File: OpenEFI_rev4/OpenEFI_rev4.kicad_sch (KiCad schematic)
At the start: 97 parts, among them J1 USB_B, J2 Tag connect, J3 104031-0811, J4 Conn_02x08_Odd_Even, Q1 AO3400A, Q11 SS8050, Q12 AO3400A, Q19 AO3400A, Q2 AO3400A, Q3 AO3400A, Q4 AO3400A, Q8 SS8050, Q9 SS8050, SW1 SW_Push, U11 SRV05-4, U15 REF3033, U23 PaP_Driver_v1, U25 TJA1051T-3, U3 STM32F407VGTx, U7 25LCxxx, Y1 25MHz, Y3 32.768kHz

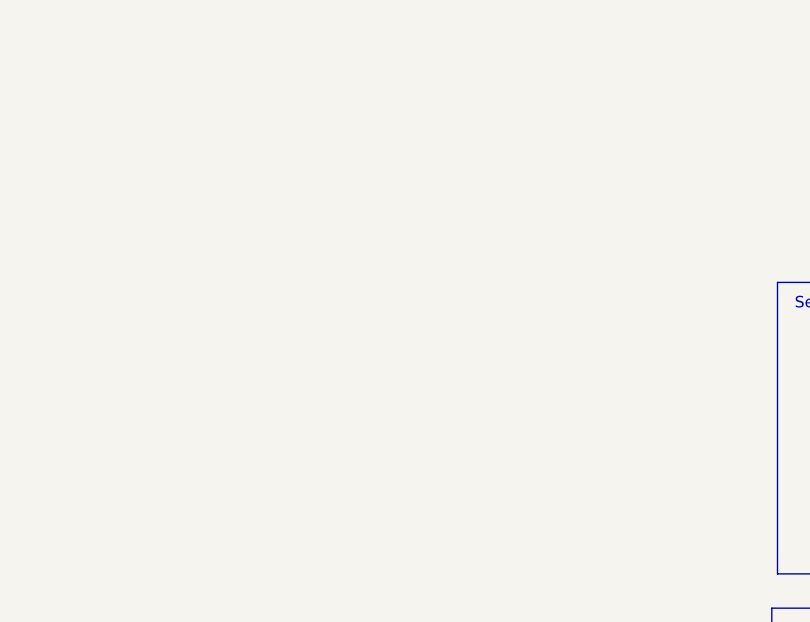
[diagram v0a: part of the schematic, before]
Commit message: fix pcb size/wideband
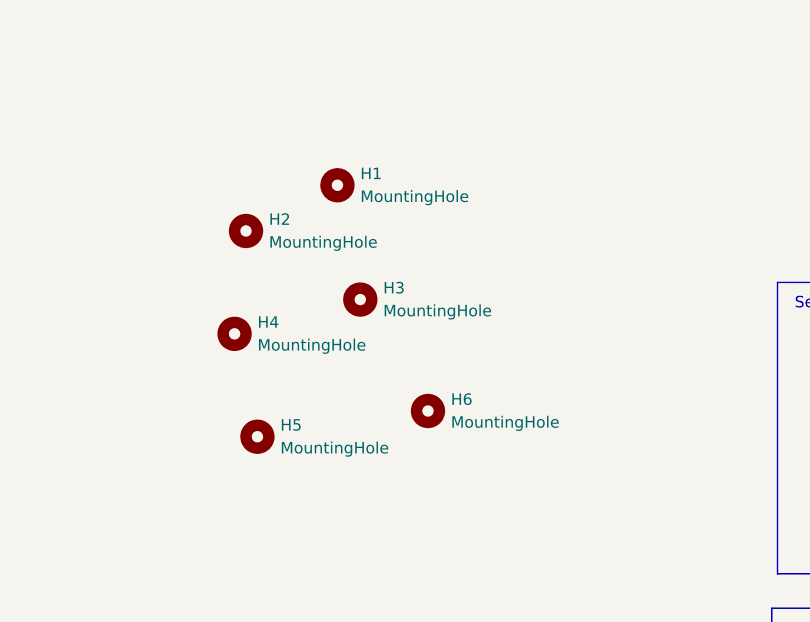
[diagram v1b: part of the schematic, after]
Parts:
- added H1, H2, H3, H4: MountingHole, MountingHole:MountingHole_3.5mm_Pad_Via, symbol Mechanical:MountingHole
- added H5, H6: MountingHole, MountingHole:MountingHole_2.1mm, symbol Mechanical:MountingHole
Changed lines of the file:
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@@
     )
   )
+  (symbol (lib_id "Mechanical:MountingHole") (at 257.81 102.87 0) (unit 1)
+    (in_bom yes) (on_board yes) (dnp no) (fields_autoplaced)
+    (property "Reference" "H3" (at 260.35 101.6 0)
+      (effects (font (size 1.27 1.27)) (justify left))
+    )
+    (property "Value" "MountingHole" (at 260.35 104.14 0)
+      (effects (font (size 1.27 1.27)) (justify left))
+    )
+    (property "Footprint" "MountingHole:MountingHole_3.5mm_Pad_Via" (at 257.81 102.87 0)
+      (effects (font (size 1.27 1.27)) hide)
+    )
+    (property "Datasheet" "~" (at 257.81 102.87 0)
+      (effects (font (size 1.27 1.27)) hide)
+    )
+    (instances
+      (project "OpenEFI_rev4"
+        (path "/b282ce4b-c3d0-4c94-b06c-73b92bb672a9"
+          (reference "H3") (unit 1)
+        )
+      )
+    )
+  )
   (symbol (lib_id "power:+3V3") (at 372.11 149.86 0) (unit 1)
     (in_bom yes) (on_board yes) (dnp no)
@@
     )
   )
+  (symbol (lib_id "Mechanical:MountingHole") (at 265.3277 115.2512 0) (unit 1)
+    (in_bom yes) (on_board yes) (dnp no) (fields_autoplaced)
+    (property "Reference" "H6" (at 267.8677 113.9812 0)
+      (effects (font (size 1.27 1.27)) (justify left))
+    )
+    (property "Value" "MountingHole" (at 267.8677 116.5212 0)
+      (effects (font (size 1.27 1.27)) (justify left))
+    )
+    (property "Footprint" "MountingHole:MountingHole_2.1mm" (at 265.3277 115.2512 0)
+      (effects (font (size 1.27 1.27)) hide)
+    )
+    (property "Datasheet" "~" (at 265.3277 115.2512 0)
+      (effects (font (size 1.27 1.27)) hide)
+    )
+    (instances
+      (project "OpenEFI_rev4"
+        (path "/b282ce4b-c3d0-4c94-b06c-73b92bb672a9"
+          (reference "H6") (unit 1)
+        )
+      )
+    )
+  )
   (symbol (lib_id "Device:R") (at 167.64 51.435 0) (mirror x) (unit 1)
     (in_bom yes) (on_board yes) (dnp no)
@@
     )
   )
+  (symbol (lib_id "Mechanical:MountingHole") (at 246.38 118.11 0) (unit 1)
+    (in_bom yes) (on_board yes) (dnp no) (fields_autoplaced)
+    (property "Reference" "H5" (at 248.92 116.84 0)
+      (effects (font (size 1.27 1.27)) (justify left))
+    )
+    (property "Value" "MountingHole" (at 248.92 119.38 0)
+      (effects (font (size 1.27 1.27)) (justify left))
+    )
+    (property "Footprint" "MountingHole:MountingHole_2.1mm" (at 246.38 118.11 0)
+      (effects (font (size 1.27 1.27)) hide)
+    )
+    (property "Datasheet" "~" (at 246.38 118.11 0)
+      (effects (font (size 1.27 1.27)) hide)
+    )
+    (instances
+      (project "OpenEFI_rev4"
+        (path "/b282ce4b-c3d0-4c94-b06c-73b92bb672a9"
+          (reference "H5") (unit 1)
+        )
+      )
+    )
+  )
   (symbol (lib_id "Connector:TestPoint") (at 321.31 206.375 0) (unit 1)
     (in_bom yes) (on_board yes) (dnp no)
@@
     )
   )
+  (symbol (lib_id "Mechanical:MountingHole") (at 245.11 95.25 0) (unit 1)
+    (in_bom yes) (on_board yes) (dnp no) (fields_autoplaced)
+    (property "Reference" "H2" (at 247.65 93.98 0)
+      (effects (font (size 1.27 1.27)) (justify left))
+    )
+    (property "Value" "MountingHole" (at 247.65 96.52 0)
+      (effects (font (size 1.27 1.27)) (justify left))
+    )
+    (property "Footprint" "MountingHole:MountingHole_3.5mm_Pad_Via" (at 245.11 95.25 0)
+      (effects (font (size 1.27 1.27)) hide)
+    )
+    (property "Datasheet" "~" (at 245.11 95.25 0)
+      (effects (font (size 1.27 1.27)) hide)
+    )
+    (instances
+      (project "OpenEFI_rev4"
+        (path "/b282ce4b-c3d0-4c94-b06c-73b92bb672a9"
+          (reference "H2") (unit 1)
+        )
+      )
+    )
+  )
   (symbol (lib_id "Jumper:SolderJumper_2_Open") (at 69.85 38.1 0) (unit 1)
     (in_bom yes) (on_board yes) (dnp no)
@@
     )
   )
+  (symbol (lib_id "Mechanical:MountingHole") (at 255.27 90.17 0) (unit 1)
+    (in_bom yes) (on_board yes) (dnp no) (fields_autoplaced)
+    (property "Reference" "H1" (at 257.81 88.9 0)
+      (effects (font (size 1.27 1.27)) (justify left))
+    )
+    (property "Value" "MountingHole" (at 257.81 91.44 0)
+      (effects (font (size 1.27 1.27)) (justify left))
+    )
+    (property "Footprint" "MountingHole:MountingHole_3.5mm_Pad_Via" (at 255.27 90.17 0)
+      (effects (font (size 1.27 1.27)) hide)
+    )
+    (property "Datasheet" "~" (at 255.27 90.17 0)
+      (effects (font (size 1.27 1.27)) hide)
+    )
+    (instances
+      (project "OpenEFI_rev4"
+        (path "/b282ce4b-c3d0-4c94-b06c-73b92bb672a9"
+          (reference "H1") (unit 1)
+        )
+      )
+    )
+  )
   (symbol (lib_id "Device:R_Pack04") (at 316.23 34.29 0) (unit 1)
     (in_bom yes) (on_board yes) (dnp no)
@@
         )
       )
+    )
+  )
+  (symbol (lib_id "Mechanical:MountingHole") (at 243.84 106.68 0) (unit 1)
+    (in_bom yes) (on_board yes) (dnp no) (fields_autoplaced)
+    (property "Reference" "H4" (at 246.38 105.41 0)
+      (effects (font (size 1.27 1.27)) (justify left))
+    )
+    (property "Value" "MountingHole" (at 246.38 107.95 0)
+      (effects (font (size 1.27 1.27)) (justify left))
+    )
+    (property "Footprint" "MountingHole:MountingHole_3.5mm_Pad_Via" (at 243.84 106.68 0)
+      (effects (font (size 1.27 1.27)) hide)
+    )
+    (property "Datasheet" "~" (at 243.84 106.68 0)
+      (effects (font (size 1.27 1.27)) hide)
+    )
+    (instances
+      (project "OpenEFI_rev4"
+        (path "/b282ce4b-c3d0-4c94-b06c-73b92bb672a9"
+          (reference "H4") (unit 1)
+        )
+      )

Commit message: WIP Rev4 SPI
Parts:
- BT1: now left out of the parts list
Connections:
- net AUX_IN_6: now also U3.93 (PB7); no longer U3.98 (PE1)
- net AUX_IN_7: now also U3.95 (PB8); no longer U3.93 (PB7)
- net AUX_IN_8: now also U3.98 (PE1); no longer U3.95 (PB8)
- net SD_CD: now also RN5.4 (R4.1); no longer RN6.2 (R2.1)
- net SD_CMD: now also RN5.1 (R1.1); no longer RN5.2 (R2.1)
- net SD_DAT1: now also RN6.2 (R2.1); no longer RN5.1 (R1.1)
- net SD_DAT2: now also RN5.3 (R3.1); no longer RN5.4 (R4.1)
- net SD_DAT3: now also RN5.2 (R2.1); no longer RN5.3 (R3.1)
- net SPI2_MISO: now also J4.8 (Pin_8); no longer J4.6 (Pin_6)
- net SPI2_MOSI: now also J4.6 (Pin_6); no longer J4.8 (Pin_8)
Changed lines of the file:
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@@
     (effects (font (size 0.889 0.889)) (justify right bottom))
   )
-  (label "SD_DAT2" (at 334.01 38.1 270) (fields_autoplaced)
+  (label "SD_DAT2" (at 331.47 38.1 270) (fields_autoplaced)
     (effects (font (size 0.7874 0.7874)) (justify right bottom))
   )
@@
     (effects (font (size 0.8 0.8)) (justify left bottom))
   )
-  (label "SPI2_MISO" (at 323.85 226.06 0) (fields_autoplaced)
+  (label "SPI2_MISO" (at 323.85 228.6 0) (fields_autoplaced)
     (effects (font (size 0.7874 0.7874)) (justify left bottom))
   )
@@
     (effects (font (size 0.7874 0.7874)) (justify left bottom))
   )
-  (label "AUX_IN_6" (at 142.24 151.13 180) (fields_autoplaced)
-    (effects (font (size 0.889 0.889)) (justify right bottom))
+  (label "AUX_IN_6" (at 193.04 166.37 0) (fields_autoplaced)
+    (effects (font (size 0.889 0.889)) (justify left bottom))
   )
   (label "MUX_A" (at 142.24 199.39 180) (fields_autoplaced)
@@
     (effects (font (size 0.7874 0.7874)) (justify left bottom))
   )
-  (label "AUX_IN_8" (at 193.04 168.91 0) (fields_autoplaced)
-    (effects (font (size 0.889 0.889)) (justify left bottom))
+  (label "AUX_IN_8" (at 142.24 151.13 180) (fields_autoplaced)
+    (effects (font (size 0.889 0.889)) (justify right bottom))
   )
   (label "ECN2" (at 401.32 118.11 180) (fields_autoplaced)
@@
     (effects (font (size 1.27 1.27)) (justify right bottom))
   )
-  (label "SPI2_MOSI" (at 323.85 228.6 0) (fields_autoplaced)
+  (label "SPI2_MOSI" (at 323.85 226.06 0) (fields_autoplaced)
     (effects (font (size 0.7874 0.7874)) (justify left bottom))
   )
@@
     (effects (font (size 0.7874 0.7874)) (justify left bottom))
   )
-  (label "SD_CMD" (at 328.93 38.1 270) (fields_autoplaced)
+  (label "SD_CMD" (at 326.39 38.1 270) (fields_autoplaced)
     (effects (font (size 0.7874 0.7874)) (justify right bottom))
   )
@@
     (effects (font (size 0.9906 0.9906)) (justify left bottom))
   )
-  (label "AUX_IN_7" (at 193.04 166.37 0) (fields_autoplaced)
+  (label "AUX_IN_7" (at 193.04 168.91 0) (fields_autoplaced)
     (effects (font (size 0.889 0.889)) (justify left bottom))
   )
@@
     (effects (font (size 0.889 0.889)) (justify left bottom))
   )
-  (label "SD_DAT1" (at 326.39 38.1 270) (fields_autoplaced)
+  (label "SD_DAT1" (at 313.69 39.37 270) (fields_autoplaced)
     (effects (font (size 0.7874 0.7874)) (justify right bottom))
   )
@@
     (effects (font (size 0.889 0.889)) (justify right bottom))
   )
-  (label "SD_DAT3" (at 331.47 38.1 270) (fields_autoplaced)
+  (label "SD_DAT3" (at 328.93 38.1 270) (fields_autoplaced)
     (effects (font (size 0.7874 0.7874)) (justify right bottom))
   )
@@
     (effects (font (size 0.9906 0.9906)) (justify left bottom))
   )
-  (label "SD_CD" (at 313.69 39.37 270) (fields_autoplaced)
+  (label "SD_CD" (at 334.01 38.1 270) (fields_autoplaced)
     (effects (font (size 0.889 0.889)) (justify right bottom))
   )
@@
     )
   )
-  (symbol (lib_id "Mechanical:MountingHole") (at 257.81 102.87 0) (unit 1)
+  (symbol (lib_id "Mechanical:MountingHole") (at 290.83 177.165 0) (unit 1)
     (in_bom yes) (on_board yes) (dnp no) (fields_autoplaced)
-    (property "Reference" "H3" (at 260.35 101.6 0)
-      (effects (font (size 1.27 1.27)) (justify left))
+    (property "Reference" "H3" (at 293.37 175.895 0)
+      (effects (font (size 1.27 1.27)) (justify left) hide)
     )
-    (property "Value" "MountingHole" (at 260.35 104.14 0)
-      (effects (font (size 1.27 1.27)) (justify left))
+    (property "Value" "MountingHole" (at 293.37 178.435 0)
+      (effects (font (size 1.27 1.27)) (justify left) hide)
     )
-    (property "Footprint" "MountingHole:MountingHole_3.5mm_Pad_Via" (at 257.81 102.87 0)
+    (property "Footprint" "MountingHole:MountingHole_3.5mm_Pad_Via" (at 290.83 177.165 0)
       (effects (font (size 1.27 1.27)) hide)
     )
-    (property "Datasheet" "~" (at 257.81 102.87 0)
+    (property "Datasheet" "~" (at 290.83 177.165 0)
       (effects (font (size 1.27 1.27)) hide)
     )
@@
     )
   )
-  (symbol (lib_id "Mechanical:MountingHole") (at 265.3277 115.2512 0) (unit 1)
+  (symbol (lib_id "Mechanical:MountingHole") (at 290.83 172.72 0) (unit 1)
     (in_bom yes) (on_board yes) (dnp no) (fields_autoplaced)
-    (property "Reference" "H6" (at 267.8677 113.9812 0)
-      (effects (font (size 1.27 1.27)) (justify left))
+    (property "Reference" "H6" (at 293.37 172.72 0)
+      (effects (font (size 1.27 1.27)) (justify left) hide)
     )
-    (property "Value" "MountingHole" (at 267.8677 116.5212 0)
-      (effects (font (size 1.27 1.27)) (justify left))
+    (property "Value" "MountingHole" (at 293.37 173.99 0)
+      (effects (font (size 1.27 1.27)) (justify left) hide)
     )
-    (property "Footprint" "MountingHole:MountingHole_2.1mm" (at 265.3277 115.2512 0)
+    (property "Footprint" "MountingHole:MountingHole_2.1mm" (at 290.83 172.72 0)
       (effects (font (size 1.27 1.27)) hide)
     )
-    (property "Datasheet" "~" (at 265.3277 115.2512 0)
+    (property "Datasheet" "~" (at 290.83 172.72 0)
       (effects (font (size 1.27 1.27)) hide)
     )
@@
     )
   )
-  (symbol (lib_id "Mechanical:MountingHole") (at 246.38 118.11 0) (unit 1)
+  (symbol (lib_id "Mechanical:MountingHole") (at 286.385 177.165 0) (unit 1)
     (in_bom yes) (on_board yes) (dnp no) (fields_autoplaced)
-    (property "Reference" "H5" (at 248.92 116.84 0)
-      (effects (font (size 1.27 1.27)) (justify left))
+    (property "Reference" "H5" (at 290.0927 177.165 0)
+      (effects (font (size 1.27 1.27)) (justify left) hide)
     )
-    (property "Value" "MountingHole" (at 248.92 119.38 0)
-      (effects (font (size 1.27 1.27)) (justify left))
+    (property "Value" "MountingHole" (at 288.925 178.435 0)
+      (effects (font (size 1.27 1.27)) (justify left) hide)
     )
-    (property "Footprint" "MountingHole:MountingHole_2.1mm" (at 246.38 118.11 0)
+    (property "Footprint" "MountingHole:MountingHole_2.1mm" (at 286.385 177.165 0)
       (effects (font (size 1.27 1.27)) hide)
     )
-    (property "Datasheet" "~" (at 246.38 118.11 0)
+    (property "Datasheet" "~" (at 286.385 177.165 0)
       (effects (font (size 1.27 1.27)) hide)
     )
@@
     )
   )
-  (symbol (lib_id "Mechanical:MountingHole") (at 245.11 95.25 0) (unit 1)
+  (symbol (lib_id "Mechanical:MountingHole") (at 286.385 168.275 0) (unit 1)
     (in_bom yes) (on_board yes) (dnp no) (fields_autoplaced)
-    (property "Reference" "H2" (at 247.65 93.98 0)
-      (effects (font (size 1.27 1.27)) (justify left))
+    (property "Reference" "H2" (at 288.925 167.005 0)
+      (effects (font (size 1.27 1.27)) (justify left) hide)
     )
-    (property "Value" "MountingHole" (at 247.65 96.52 0)
-      (effects (font (size 1.27 1.27)) (justify left))
+    (property "Value" "MountingHole" (at 288.925 169.545 0)
+      (effects (font (size 1.27 1.27)) (justify left) hide)
     )
-    (property "Footprint" "MountingHole:MountingHole_3.5mm_Pad_Via" (at 245.11 95.25 0)
+    (property "Footprint" "MountingHole:MountingHole_3.5mm_Pad_Via" (at 286.385 168.275 0)
       (effects (font (size 1.27 1.27)) hide)
     )
-    (property "Datasheet" "~" (at 245.11 95.25 0)
+    (property "Datasheet" "~" (at 286.385 168.275 0)
       (effects (font (size 1.27 1.27)) hide)
     )
@@
     )
   )
-  (symbol (lib_id "Mechanical:MountingHole") (at 255.27 90.17 0) (unit 1)
+  (symbol (lib_id "Mechanical:MountingHole") (at 290.83 168.275 0) (unit 1)
     (in_bom yes) (on_board yes) (dnp no) (fields_autoplaced)
-    (property "Reference" "H1" (at 257.81 88.9 0)
-      (effects (font (size 1.27 1.27)) (justify left))
+    (property "Reference" "H1" (at 293.37 167.005 0)
+      (effects (font (size 1.27 1.27)) (justify left) hide)
     )
-    (property "Value" "MountingHole" (at 257.81 91.44 0)
-      (effects (font (size 1.27 1.27)) (justify left))
+    (property "Value" "MountingHole" (at 293.37 169.545 0)
+      (effects (font (size 1.27 1.27)) (justify left) hide)
     )
-    (property "Footprint" "MountingHole:MountingHole_3.5mm_Pad_Via" (at 255.27 90.17 0)
+    (property "Footprint" "MountingHole:MountingHole_3.5mm_Pad_Via" (at 290.83 168.275 0)
       (effects (font (size 1.27 1.27)) hide)
     )
-    (property "Datasheet" "~" (at 255.27 90.17 0)
+    (property "Datasheet" "~" (at 290.83 168.275 0)
       (effects (font (size 1.27 1.27)) hide)
     )
@@
   )
   (symbol (lib_id "Device:Battery_Cell") (at 151.13 92.71 0) (unit 1)
-    (in_bom yes) (on_board yes) (dnp no) (fields_autoplaced)
+    (in_bom no) (on_board yes) (dnp no) (fields_autoplaced)
     (property "Reference" "BT1" (at 154.94 89.5985 0)
       (effects (font (size 1.27 1.27)) (justify left))
@@
     )
   )
-  (symbol (lib_id "Mechanical:MountingHole") (at 243.84 106.68 0) (unit 1)
+  (symbol (lib_id "Mechanical:MountingHole") (at 286.385 172.72 0) (unit 1)
     (in_bom yes) (on_board yes) (dnp no) (fields_autoplaced)
-    (property "Reference" "H4" (at 246.38 105.41 0)
-      (effects (font (size 1.27 1.27)) (justify left))
+    (property "Reference" "H4" (at 288.925 171.45 0)
+      (effects (font (size 1.27 1.27)) (justify left) hide)
     )
-    (property "Value" "MountingHole" (at 246.38 107.95 0)
-      (effects (font (size 1.27 1.27)) (justify left))
+    (property "Value" "MountingHole" (at 288.925 173.99 0)
+      (effects (font (size 1.27 1.27)) (justify left) hide)
     )
-    (property "Footprint" "MountingHole:MountingHole_3.5mm_Pad_Via" (at 243.84 106.68 0)
+    (property "Footprint" "MountingHole:MountingHole_3.5mm_Pad_Via" (at 286.385 172.72 0)
       (effects (font (size 1.27 1.27)) hide)
     )
-    (property "Datasheet" "~" (at 243.84 106.68 0)
+    (property "Datasheet" "~" (at 286.385 172.72 0)
       (effects (font (size 1.27 1.27)) hide)
     )

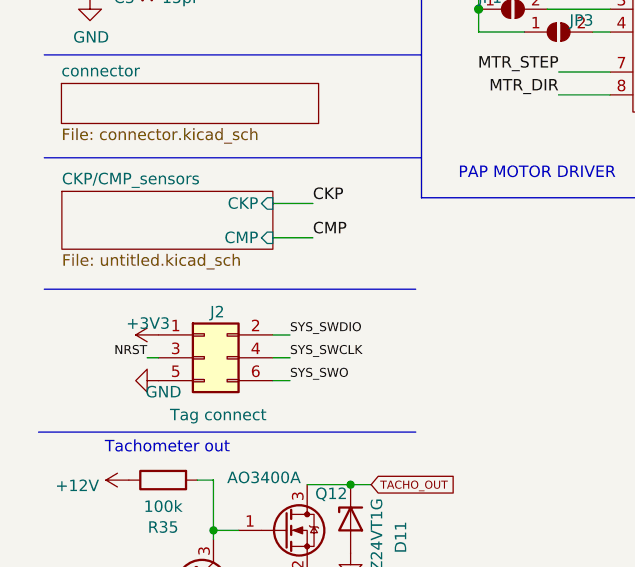
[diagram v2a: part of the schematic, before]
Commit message: Rev4: add all MCU signals
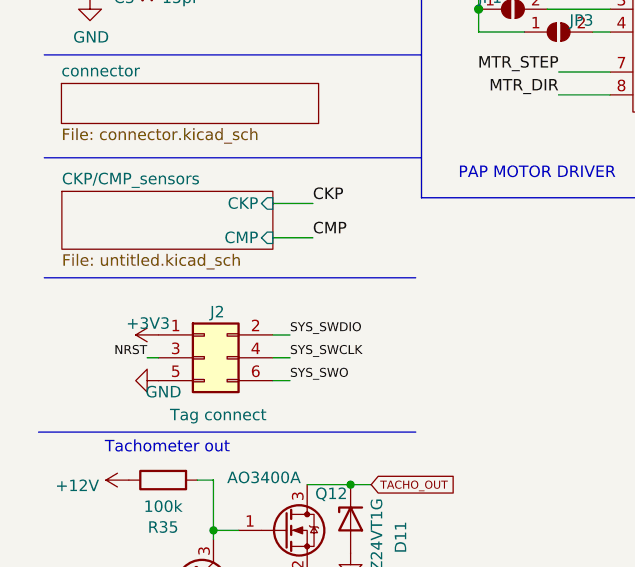
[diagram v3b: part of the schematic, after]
